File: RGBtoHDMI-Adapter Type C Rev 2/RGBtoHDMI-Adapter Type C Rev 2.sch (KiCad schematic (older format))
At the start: 5 parts, among them J1 Conn_02x20_Odd_Even, J2 Conn_02x20_Odd_Even

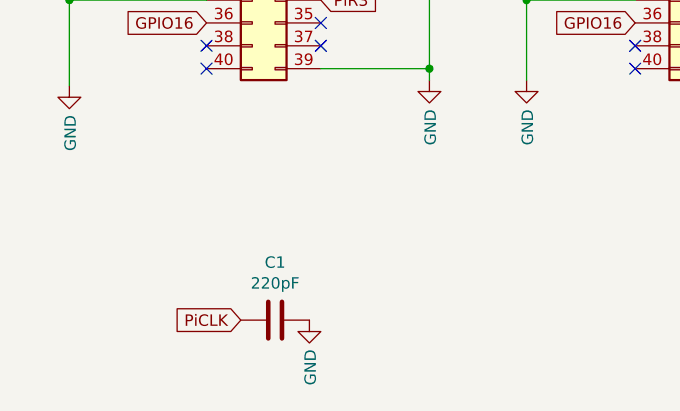
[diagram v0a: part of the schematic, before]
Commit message: Updated cap value to 47pF
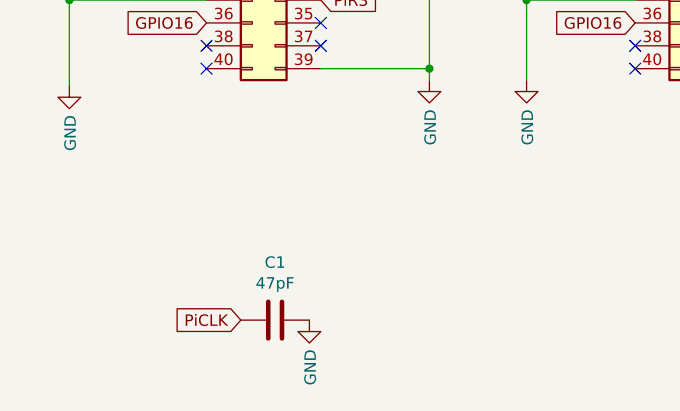
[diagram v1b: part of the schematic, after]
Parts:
- C1: value 220pF -> 47pF
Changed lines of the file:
@@
 P 4625 5050
 F 0 "C1" V 4373 5050 50  0000 C CNN
-F 1 "220pF" V 4464 5050 50  0000 C CNN
+F 1 "47pF" V 4464 5050 50  0000 C CNN
 F 2 "Capacitor_SMD:C_0805_2012Metric_Pad1.18x1.45mm_HandSolder" H 4663 4900 50  0001 C CNN
 F 3 "~" H 4625 5050 50  0001 C CNN
